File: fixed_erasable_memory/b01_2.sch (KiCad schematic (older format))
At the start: 27 parts, among them U13030 74HC02, U13033 74HC02, U13035 74HC02, U13037 74HC04, U31013 74HC4002, U31016 74HC04, U31018 74HC02, U31019 74HC4002, U31020 74HC4002, U31021 74HC4002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

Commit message: New bidirectional codegen flags for the MRAM chip.
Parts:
- U31025: FPGA#bidir (none) -> 7,8,9,10,13,14,15,16,29,30,31,32,35,36,37,38
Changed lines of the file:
@@
 F 2 "" H 19000 5350 60  0000 C CNN
 F 3 "" H 19000 5350 60  0000 C CNN
+F 4 "7,8,9,10,13,14,15,16,29,30,31,32,35,36,37,38" H 19000 5050 60  0001 C CNN "FPGA#bidir"
 	1    19000 5050
 	1    0    0    -1

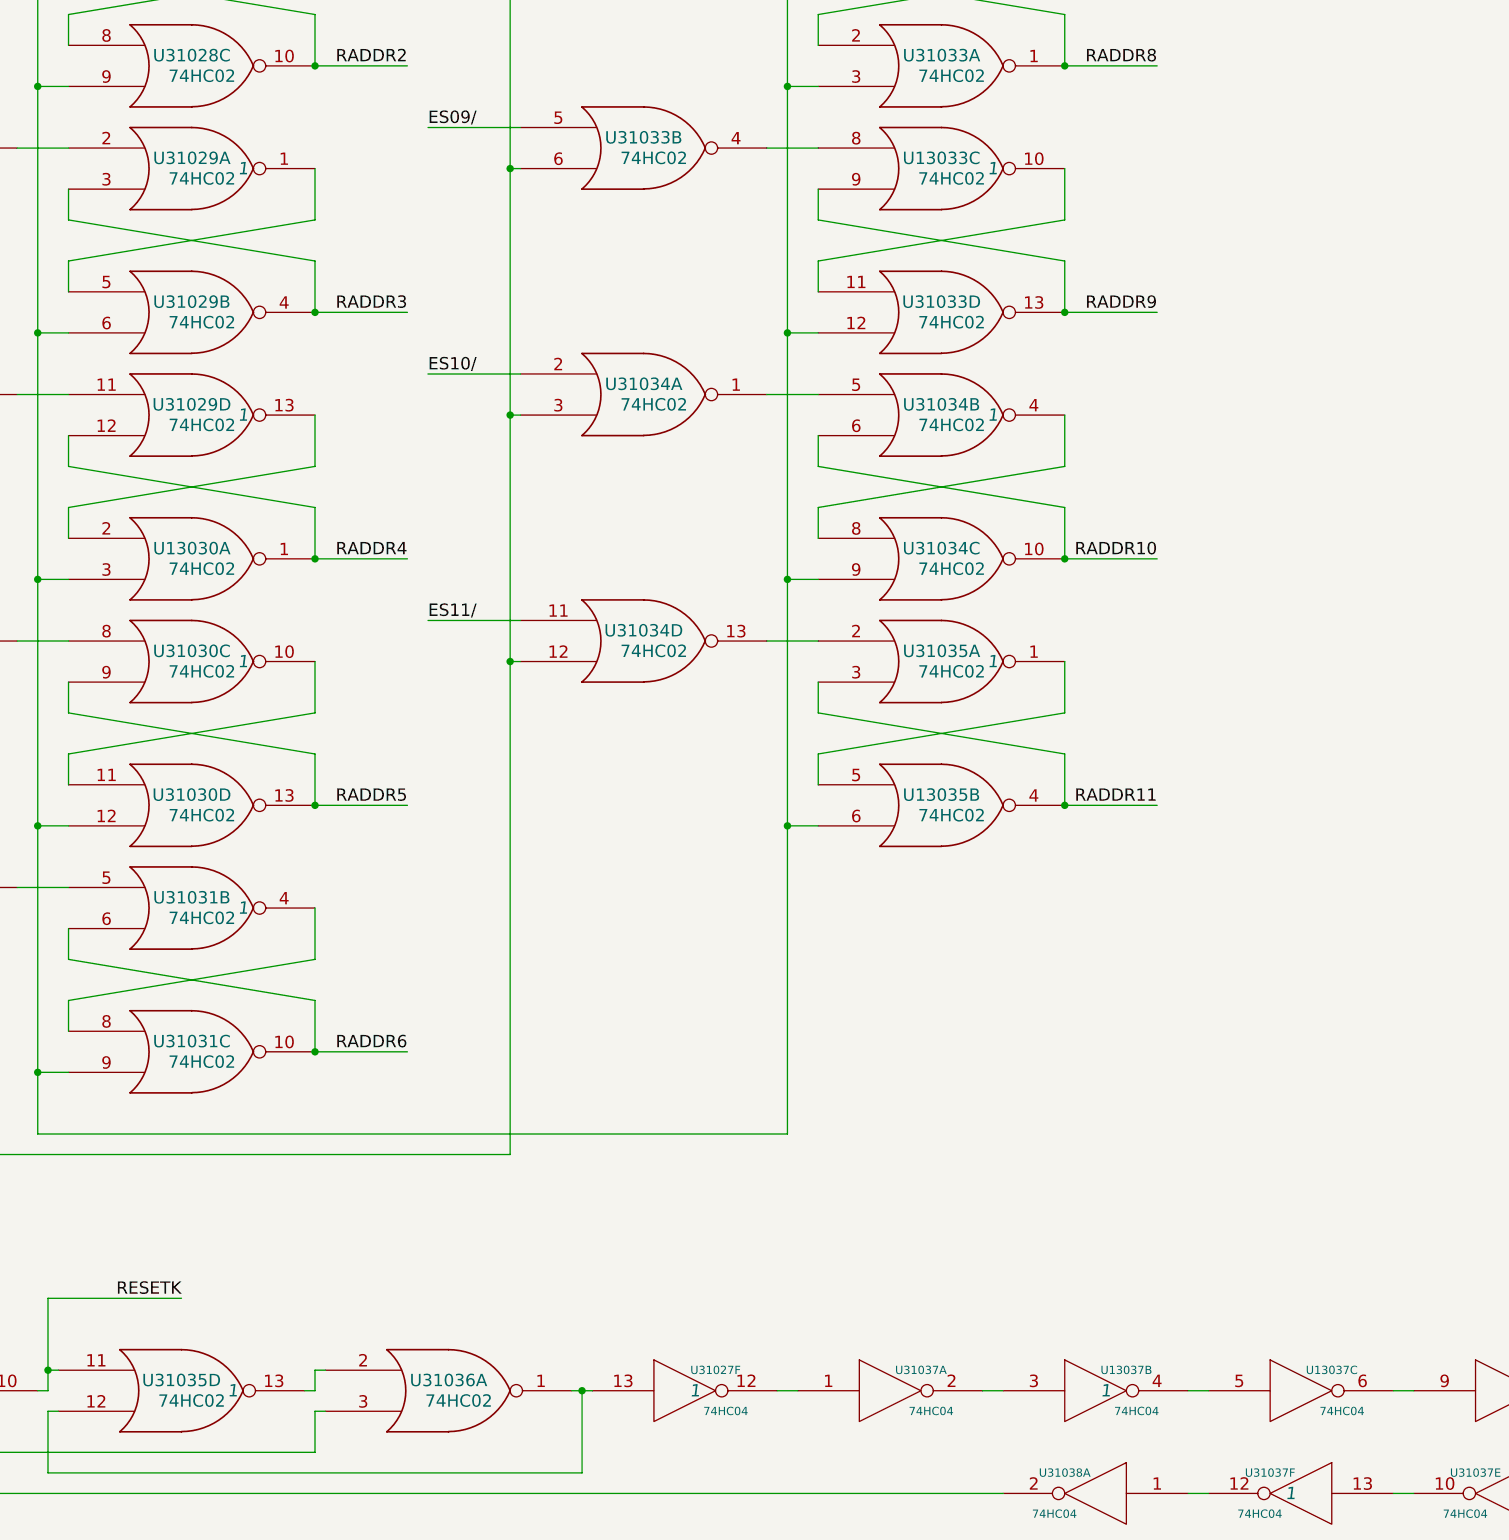
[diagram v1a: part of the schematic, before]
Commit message: Corrected some bad identifiers found by Quartus
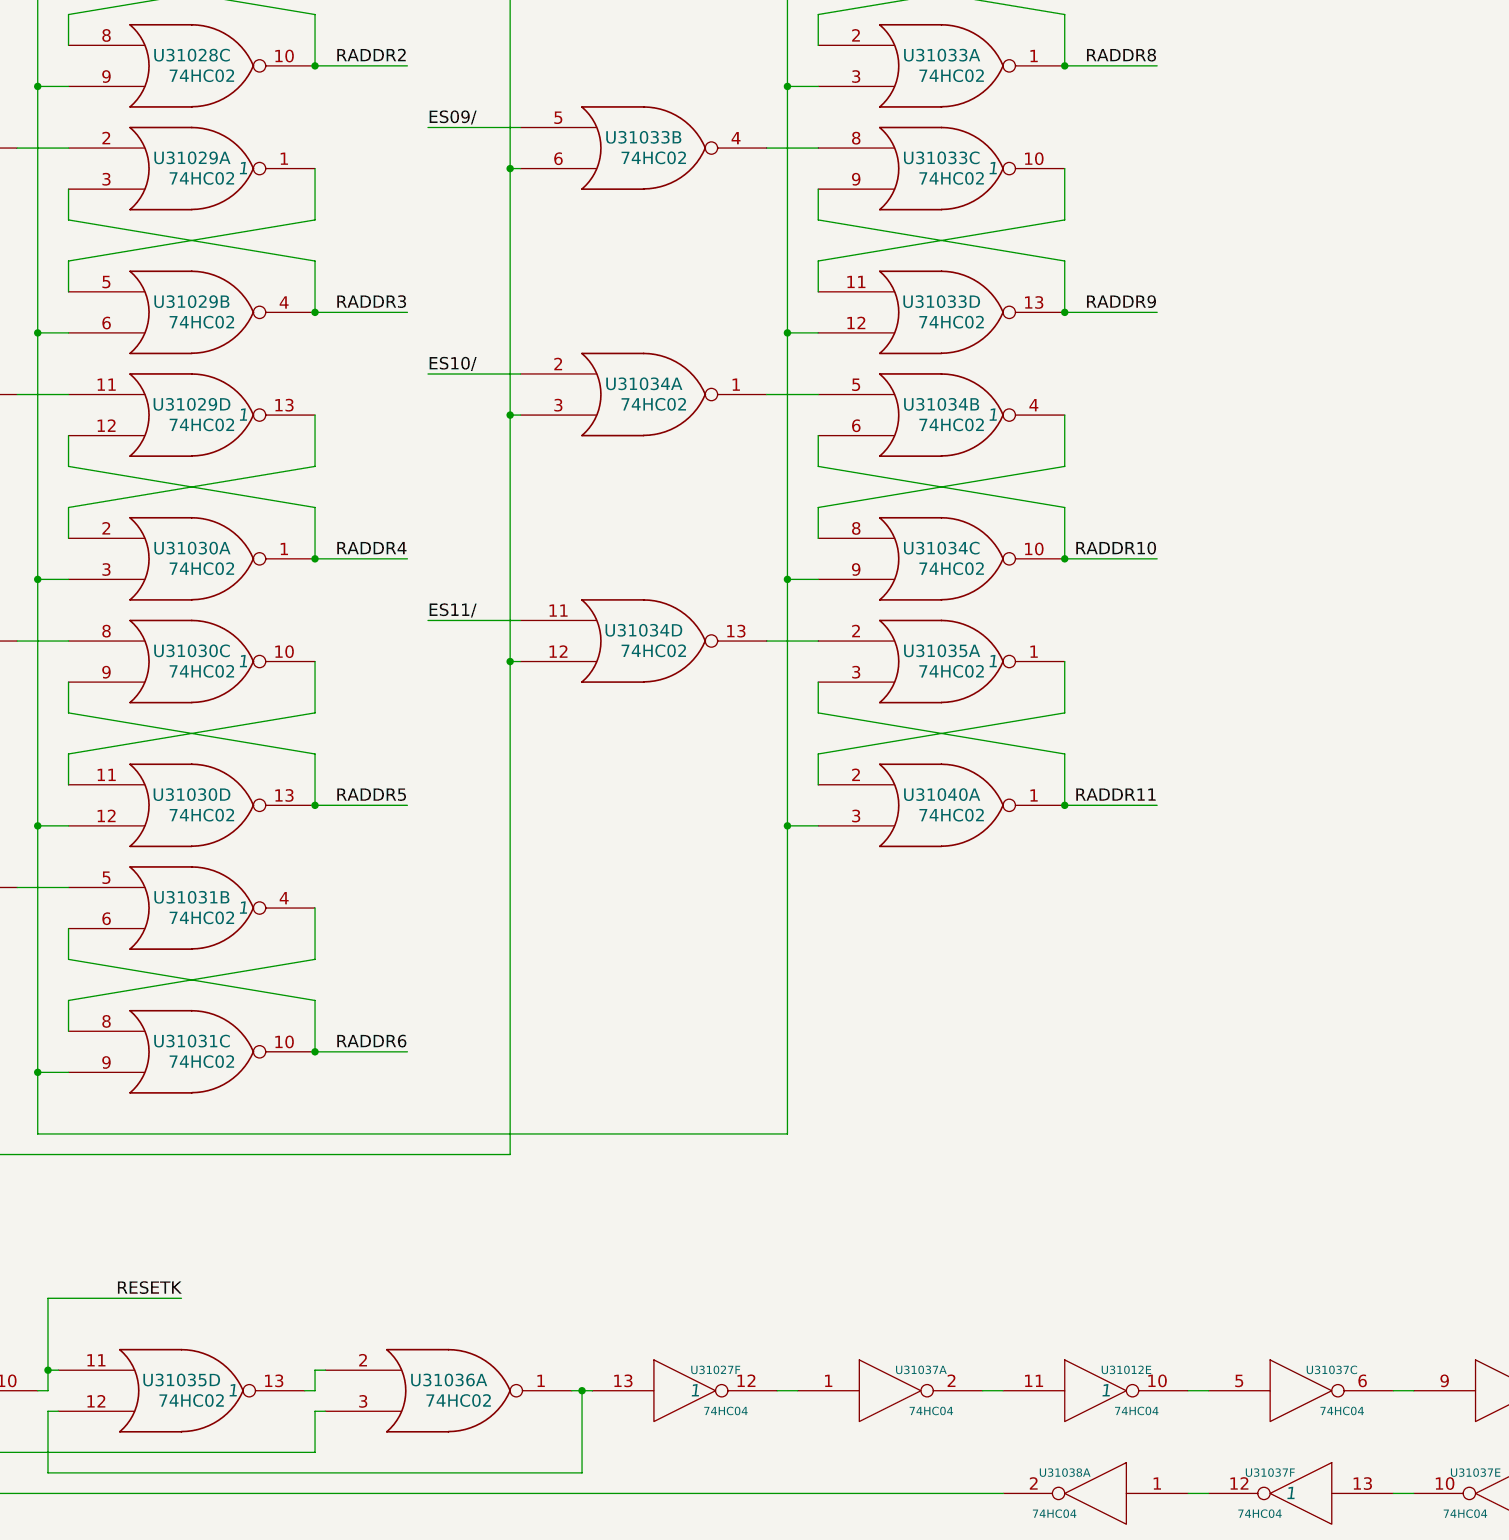
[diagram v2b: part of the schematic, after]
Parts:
- renumbered U13037 to U31012, U13030 to U31030, U13033 to U31033, U13037 to U31037, U13035 to U31040
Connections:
- net RADDR11: now also U31040.1; no longer U31040.4
- net RESETK: now also U31040.3; no longer U31040.6
- net at U31035.1: now also U31040.2; no longer U31040.5
- net at U31037.2: now also U31012.11; no longer U31012.3
- net at U31037.5: now also U31012.10; no longer U31012.4
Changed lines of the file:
@@
 $EndComp
 $Comp
-L 74HC02 U13030
+L 74HC02 U31030
 U 1 1 56E7E073
 P 7500 5250
-F 0 "U13030" H 7500 5300 60  0000 C CNN
+F 0 "U31030" H 7500 5300 60  0000 C CNN
 F 1 "74HC02" H 7550 5200 60  0000 C CNN
 F 2 "" H 7500 5250 60  0000 C CNN
@@
 $EndComp
 $Comp
-L 74HC02 U13033
+L 74HC02 U31033
 U 3 1 56E82D14
 P 11150 3350
-F 0 "U13033" H 11150 3400 60  0000 C CNN
+F 0 "U31033" H 11150 3400 60  0000 C CNN
 F 1 "74HC02" H 11200 3300 60  0000 C CNN
 F 2 "" H 11150 3350 60  0000 C CNN
@@
 $EndComp
 $Comp
-L 74HC02 U13035
-U 2 1 56E82F77
+L 74HC02 U31040
+U 1 1 56E82F77
 P 11150 6450
-F 0 "U13035" H 11150 6500 60  0000 C CNN
+F 0 "U31040" H 11150 6500 60  0000 C CNN
 F 1 "74HC02" H 11200 6400 60  0000 C CNN
 F 2 "" H 11150 6450 60  0000 C CNN
 F 3 "" H 11150 6450 60  0000 C CNN
-	2    11150 6450
+	1    11150 6450
 	1    0    0    -1
 $EndComp
@@
 Connection ~ 9400 9300
 $Comp
-L 74HC04 U13037
-U 2 1 56E9D326
+L 74HC04 U31012
+U 5 1 56E9D326
 P 11900 9300
-F 0 "U13037" H 12050 9400 40  0000 C CNN
+F 0 "U31012" H 12050 9400 40  0000 C CNN
 F 1 "74HC04" H 12100 9200 40  0000 C CNN
 F 2 "" H 11900 9300 60  0000 C CNN
 F 3 "" H 11900 9300 60  0000 C CNN
 F 4 "1" H 11950 9300 60  0000 C CIN "Initial"
-	2    11900 9300
+	5    11900 9300
 	1    0    0    -1
 $EndComp
@@
 	11350 9300 11450 9300
 $Comp
-L 74HC04 U13037
+L 74HC04 U31037
 U 3 1 56E9D32E
 P 12900 9300
-F 0 "U13037" H 13050 9400 40  0000 C CNN
+F 0 "U31037" H 13050 9400 40  0000 C CNN
 F 1 "74HC04" H 13100 9200 40  0000 C CNN
 F 2 "" H 12900 9300 60  0000 C CNN

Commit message: Made erasable memory reads destructive, and improved erasable address latching logic
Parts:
- added U31008: 74HC27, symbol 74HC27
- added unit 2 of U31040
- added unit 3 of U31040
- U31027: Initial 1 -> (none)
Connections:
- net GND: now also U31008.7 (GND), U31040.7 (GND), U31040.7 (GND)
- net RESETK: now also U31008.6; no longer U31035.10, U31035.11
- net VCC: now also U31008.14 (VCC), U31040.14 (VCC), U31040.14 (VCC)
- net ZID: now also U31008.5
- net at U31025.17 (W#): now also U31040.10; no longer U31027.6
- net at U31026.1: now also U31040.8; no longer U31027.5
- net at U31026.6, U31027.10, U31028.12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: no longer U31035.8, U31036.3
- new net: U31027.6, U31035.8, U31036.3
- new net: U31027.5, U31040.4
- new net EDESTROY: U31035.10, U31035.11, U31040.9
- new net REX: U31040.5
- new net REY: U31040.6
- new net RSTKX/: U31008.3
- new net RSTKY/: U31008.4
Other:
- moved on the sheet: U31012E, U31026A, U31026B, U31026C, U31026D, U31027A, U31027B, U31027E, U31027F, U31028A, U31028B, U31028C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

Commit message: Fixed not->1-input nor in the rest of the modules.
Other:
- moved on the sheet: U31012E, U31016F, U31027A, U31027B, U31027D, U31027E, U31027F, U31037A, U31037C, U31037D, U31037E, U31037F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

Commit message: Fixed/erasable memory on switched power, and voltage pin updates for the memories and tristate buffers
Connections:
- net labels added: +4VSW
- wire segments 317 -> 329
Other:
- moved on the sheet: U31016F, U31023, U31024
